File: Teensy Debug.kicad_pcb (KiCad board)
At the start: 2 copper layers, 33.5 x 19.3 mm, 3 parts, among them J1 Conn_02x07_Odd_Even, U1 MKL02Z32VFG4, U2 MKL02Z32VFG4

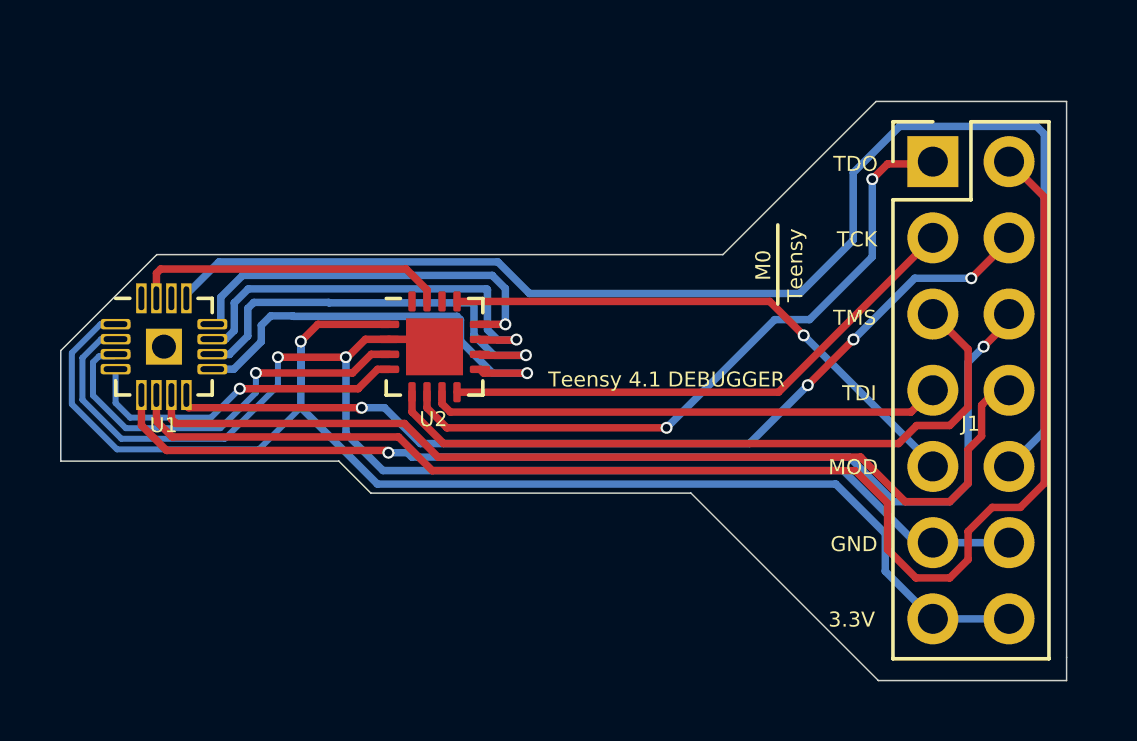
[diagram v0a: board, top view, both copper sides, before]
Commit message: V2
Changed from generic header to Cortex-M 9 pin debug header.
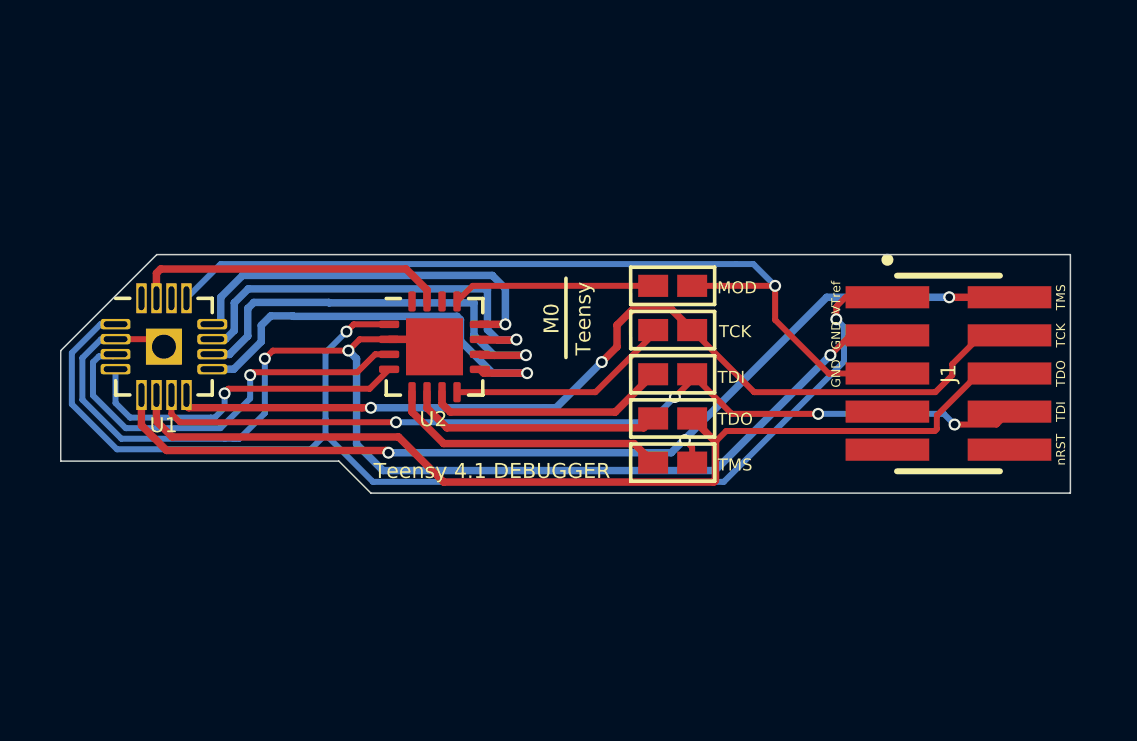
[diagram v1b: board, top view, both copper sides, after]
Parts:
- added JP1: SolderJumper_2_Open, SolderJumper:SolderJumper-2_P1.3mm_Open_Pad1.0x0.74mm, F.Cu at (133.0, 99.9)
- added JP2: SolderJumper_2_Open, SolderJumper:SolderJumper-2_P1.3mm_Open_Pad1.0x0.74mm, F.Cu at (133.0, 97.0)
- added JP3: SolderJumper_2_Open, SolderJumper:SolderJumper-2_P1.3mm_Open_Pad1.0x0.74mm, F.Cu at (133.0, 101.4)
- added JP4: SolderJumper_2_Open, SolderJumper:SolderJumper-2_P1.3mm_Open_Pad1.0x0.74mm, F.Cu at (133.0, 98.5)
- added JP5: SolderJumper_2_Open, SolderJumper:SolderJumper-2_P1.3mm_Open_Pad1.0x0.74mm, F.Cu at (133.0, 95.5)
- J1: value Conn_02x07_Odd_Even -> FTSH-105-XX-X-DV; footprint Connector_PinHeader_2.54mm:PinHeader_2x07_P2.54mm_Vertical -> SAMTEC_FTSH-105-XX-X-DV
- moved J1 7.08 mm to (142.2, 98.4), turned to 270 degrees
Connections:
- U1 pad 1: Net-(J1-Pad13) -> Net-(J1-Pad01)
- U1 pad 13: Net-(J1-Pad10) -> Net-(J1-Pad05)
- U1 pad 17: Net-(U1-Pad17) -> Net-(J1-Pad03)
- U1 pad 2: Net-(J1-Pad11) -> Net-(J1-Pad03)
- U1 pad 5: Net-(J1-Pad6) -> Net-(J1-Pad02)
- U1 pad 6: Net-(J1-Pad2) -> Net-(J1-Pad06)
- U1 pad 7: Net-(J1-Pad8) -> Net-(J1-Pad08)
- U1 pad 8: Net-(J1-Pad4) -> Net-(J1-Pad04)
- U2 pad 1: Net-(J1-Pad13) -> Net-(J1-Pad01)
- U2 pad 13: Net-(J1-Pad9) -> Net-(JP5-Pad1)
- U2 pad 17: Net-(J1-Pad11) -> Net-(J1-Pad03)
- U2 pad 2: Net-(J1-Pad11) -> Net-(J1-Pad03)
- U2 pad 5: Net-(J1-Pad5) -> Net-(JP3-Pad1)
- U2 pad 6: Net-(J1-Pad1) -> Net-(JP1-Pad1)
- U2 pad 7: Net-(J1-Pad7) -> Net-(JP4-Pad1)
- U2 pad 8: Net-(J1-Pad3) -> Net-(JP2-Pad1)
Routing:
- net Net-(J1-Pad13): track 47.8 -> 0.00 mm, vias 1 -> 0
- net Net-(J1-Pad2): track 46.5 -> 0.00 mm
- net Net-(J1-Pad10): track 44.8 -> 0.00 mm
- net Net-(J1-Pad11): track 43.2 -> 0.00 mm, vias 2 -> 0
- net Net-(J1-Pad03): track 0.00 -> 42.5 mm, vias 0 -> 3
- net Net-(J1-Pad01): track 0.00 -> 41.5 mm, vias 0 -> 2
- net Net-(J1-Pad6): track 36.0 -> 0.00 mm, vias 2 -> 0
- net Net-(J1-Pad06): track 0.00 -> 34.6 mm
- net Net-(J1-Pad02): track 0.00 -> 33.3 mm, vias 0 -> 3
- net Net-(J1-Pad8): track 32.6 -> 0.00 mm
- net Net-(J1-Pad04): track 0.00 -> 31.7 mm, vias 0 -> 2
- net Net-(J1-Pad4): track 31.3 -> 0.00 mm, vias 4 -> 0
- net Net-(J1-Pad08): track 0.00 -> 30.4 mm, vias 0 -> 4
- net Net-(J1-Pad05): track 0.00 -> 28.8 mm, vias 0 -> 1
- net Net-(J1-Pad5): track 23.7 -> 0.00 mm
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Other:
- board size 33.5 x 19.3 mm -> 33.7 x 8 mm
- rule via_min_drill: 0.3 -> 0.254
- board text added: "VTref"
- board text added: "nRST"
- board text removed: "3.3V"

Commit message: Changed through hole connection to surface mount
Through hole connection has been replaced with surface mount pads in favor of hot air installation.
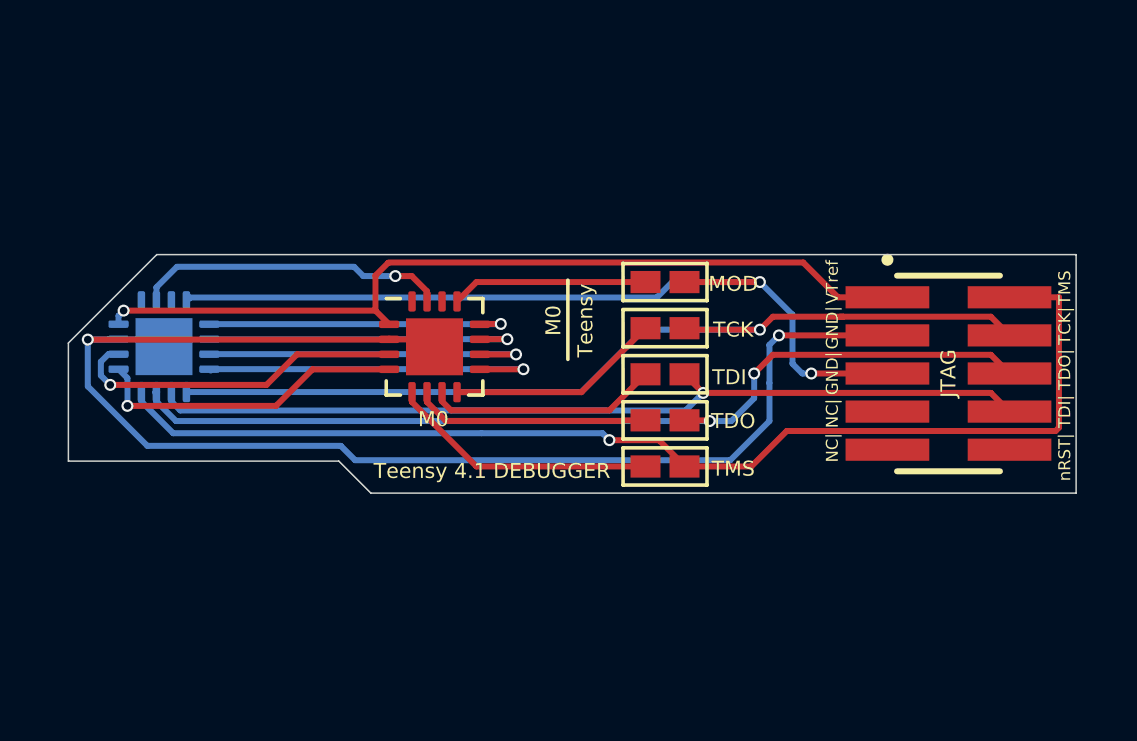
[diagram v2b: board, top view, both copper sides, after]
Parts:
- Teensy: renamed from U1; moved to B.Cu
- moved JP3 0.28 mm to (132.8, 101.5)
- moved JP5 0.28 mm to (132.8, 95.4)
- moved JP1 0.26 mm to (132.8, 100.0)
- moved JP2 0.26 mm to (132.8, 96.9)
- moved JP4 0.25 mm to (132.8, 98.5)
- renumbered J1 to JTAG, U2 to M0
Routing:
- net Net-(J1-Pad01): track 41.5 -> 28.5 mm, vias 2 -> 1
- net Net-(J1-Pad02): track 33.3 -> 38.3 mm, vias 3 -> 1
- net Net-(J1-Pad03): track 42.5 -> 47.1 mm, vias 3 -> 2
- net Net-(U1-Pad11): track 14.0 -> 10.9 mm
- net Net-(U1-Pad10): track 14.6 -> 11.4 mm
- net Net-(J1-Pad06): track 34.6 -> 31.6 mm, vias 0 -> 2
- net Net-(U1-Pad12): track 13.1 -> 10.4 mm
- net Net-(U1-Pad3): track 13.8 -> 11.3 mm
- net Net-(U1-Pad9): track 14.3 -> 12.0 mm
- net Net-(U1-Pad4): track 11.4 -> 10.6 mm
- net Net-(J1-Pad08): track 30.4 -> 29.8 mm, vias 4 -> 1
- net Net-(JP5-Pad1): track 7.15 -> 6.55 mm
- net Net-(JP1-Pad1): track 8.46 -> 7.88 mm
- net Net-(J1-Pad05): track 28.8 -> 28.4 mm, vias 1 -> 2
- net Net-(J1-Pad04): track 31.7 -> 31.4 mm, vias 2 -> 1
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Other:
- board size 33.7 x 8 mm -> 33.6 x 8 mm
- board text added: "GND|"
- board text added: "NC|"
- board text added: "TCK|"
- board text added: "TDI|"
- board text added: "TDO|"
- board text added: "nRST|"
- board text removed: "GND"
- board text removed: "nRST"

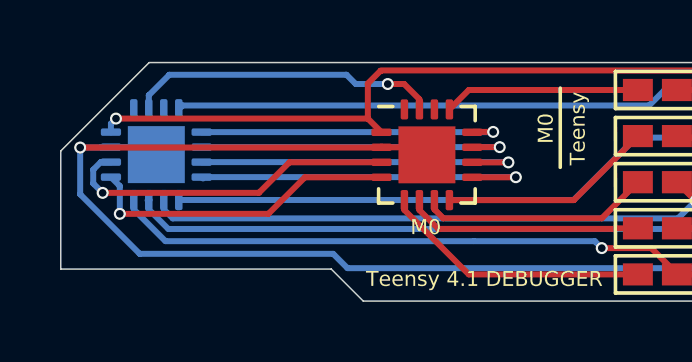
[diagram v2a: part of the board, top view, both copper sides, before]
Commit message: Revision 5
Added revision, middle ground pad resized, cleaned up a few wires, updated labels for readability.
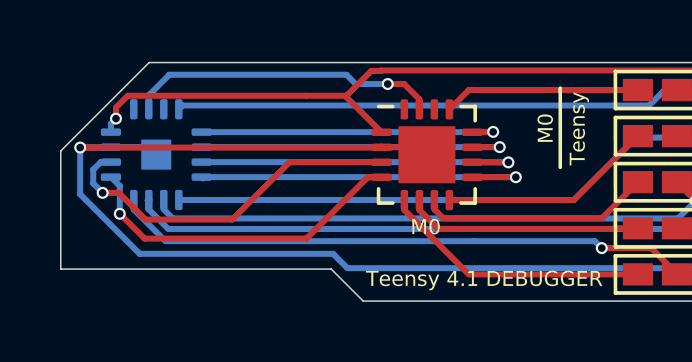
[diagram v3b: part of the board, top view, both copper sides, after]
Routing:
- net Net-(U1-Pad3): track 11.3 -> 12.1 mm
- net Net-(U1-Pad4): track 10.6 -> 11.3 mm
- net Net-(J1-Pad01): track 28.5 -> 29.0 mm
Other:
- board text added: "Revision 5"

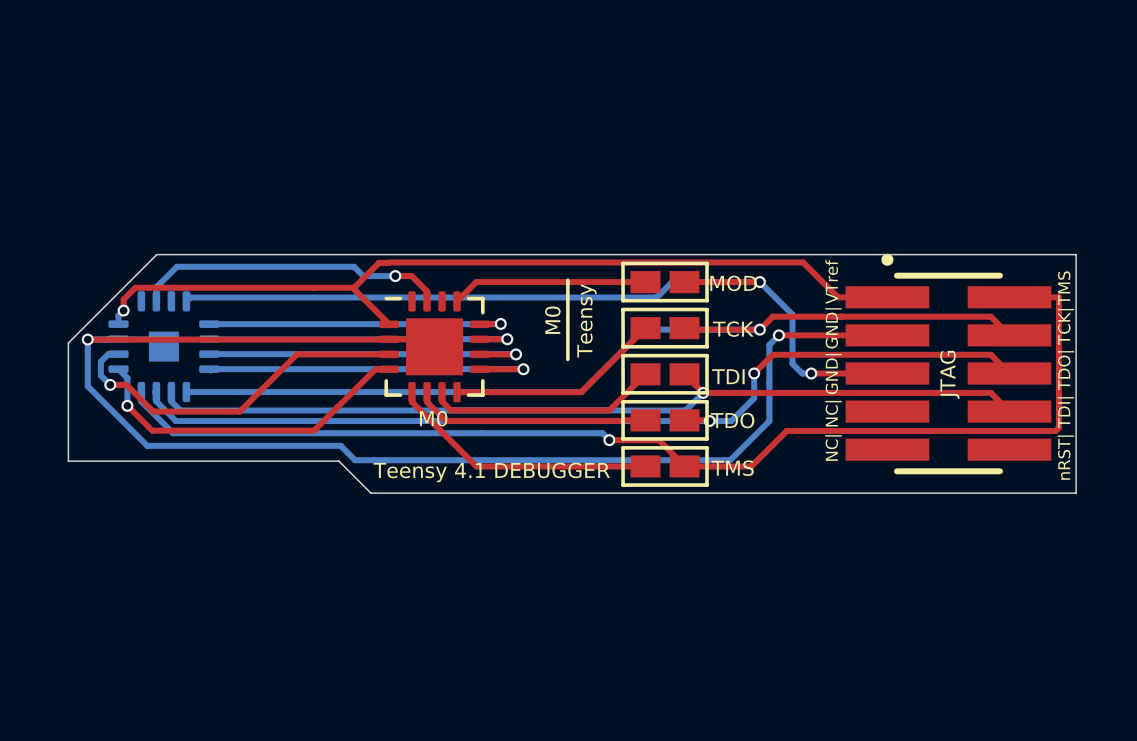
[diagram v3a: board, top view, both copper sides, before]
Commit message: Mini Version
Removed Cortex M0, replaced with Attiny10, flex pcb fits within the size of the Teensy 4.1
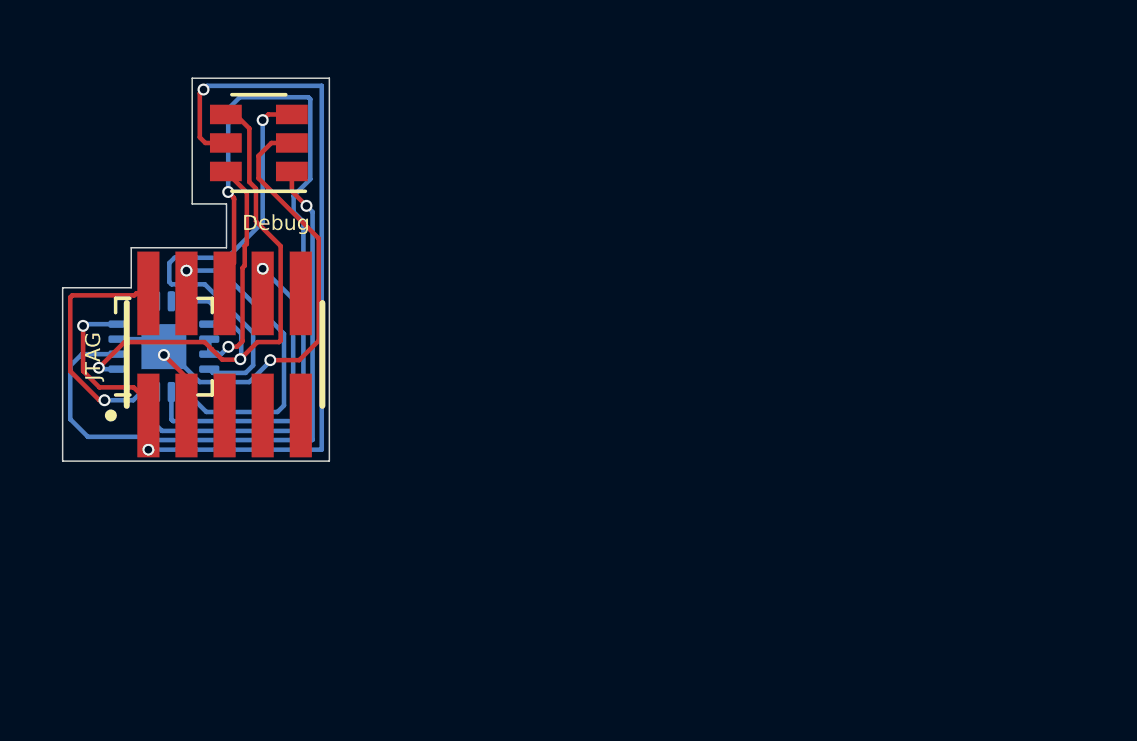
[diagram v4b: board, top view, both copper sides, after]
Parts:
- removed JP1, JP2, JP3, JP4, JP5: SolderJumper_2_Open, SolderJumper:SolderJumper-2_P1.3mm_Open_Pad1.0x0.74mm
- removed M0: MKL02Z32VFG4, Package_DFN_QFN:QFN-16-1EP_3x3mm_P0.5mm_EP1.9x1.9mm
- added U2: ATtiny10-TS, Package_TO_SOT_SMD:SOT-23-6, F.Cu at (119.3, 90.7)
- moved J1 24.1 mm to (118.1, 97.8), turned to 0 degrees
- renumbered JTAG to J1, Teensy to U1
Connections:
- J1 pad 05: Net-(J1-Pad05) -> (no net)
- J1 pad 07: Net-(J1-Pad07) -> (no net)
- J1 pad 09: Net-(J1-Pad09) -> (no net)
- J1 pad 10: Net-(J1-Pad10) -> (no net)
- U1 pad 11: Net-(U1-Pad11) -> Net-(U1-Pad10)
- U1 pad 12: Net-(U1-Pad12) -> (no net)
- U1 pad 13: Net-(J1-Pad05) -> Net-(U1-Pad13)
- U1 pad 14: Net-(U1-Pad14) -> (no net)
- U1 pad 15: Net-(U1-Pad15) -> (no net)
- U1 pad 16: Net-(U1-Pad16) -> (no net)
- U1 pad 4: Net-(U1-Pad4) -> Net-(U1-Pad13)
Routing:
- net Net-(J1-Pad02): track 38.3 -> 8.07 mm
- net Net-(J1-Pad03): track 47.1 -> 17.8 mm
- net Net-(J1-Pad05): track 28.4 -> 0.00 mm, vias 2 -> 0
- net Net-(J1-Pad04): track 31.4 -> 10.1 mm
- net Net-(J1-Pad08): track 29.8 -> 10.5 mm
- net Net-(U1-Pad13): track 0.00 -> 19.2 mm, vias 0 -> 2
- net Net-(U1-Pad4): track 11.3 -> 0.00 mm, vias 1 -> 0
- net Net-(U1-Pad11): track 10.9 -> 0.00 mm, vias 1 -> 0
- net Net-(U1-Pad15): track 10.4 -> 0.00 mm, vias 1 -> 0
- net Net-(U1-Pad12): track 10.4 -> 0.00 mm, vias 1 -> 0
- net Net-(U1-Pad3): track 12.1 -> 21.1 mm
- net Net-(JP3-Pad1): track 9.00 -> 0.00 mm
- net Net-(JP1-Pad1): track 7.88 -> 0.00 mm
- net Net-(JP4-Pad1): track 7.71 -> 0.00 mm
- net Net-(JP2-Pad1): track 7.17 -> 0.00 mm
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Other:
- board size 33.6 x 8 mm -> 8.9 x 12.8 mm
- rule trace_min: 0.2 -> 0.1524
- board text added: "Debug"
- board text added: "JTAG"
- board text added: "Rev 6"
- board text removed: "GND|"
- board text removed: "M0"
- board text removed: "MOD"
- board text removed: "NC|"
- board text removed: "Revision 5"
- board text removed: "TCK"
- board text removed: "TCK|"
- board text removed: "TDI"
- board text removed: "TDI|"
- board text removed: "TDO"
- board text removed: "TDO|"
- board text removed: "TMS"
- board text removed: "Teensy"
- board text removed: "VTref"
- board text removed: "nRST|"

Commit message: V2 Mini
Current version
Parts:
- added REF**: Teensy 4.1, teensy:Teensy41, F.Cu at (112.9, 118.5)
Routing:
- net Net-(J1-Pad06): track 28.4 -> 23.1 mm
- net Net-(J1-Pad02): track 8.07 -> 5.37 mm
- net Net-(U1-Pad3): track 21.1 -> 18.8 mm
- net Net-(J1-Pad03): track 17.8 -> 16.9 mm
- net Net-(J1-Pad01): track 30.3 -> 29.6 mm, vias 3 -> 2
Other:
- board size 8.9 x 12.8 mm -> 8.7 x 17.1 mm
- board text added: "Rev 7"
- board text removed: "Rev 6"
